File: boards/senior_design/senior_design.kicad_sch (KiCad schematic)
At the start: 55 parts

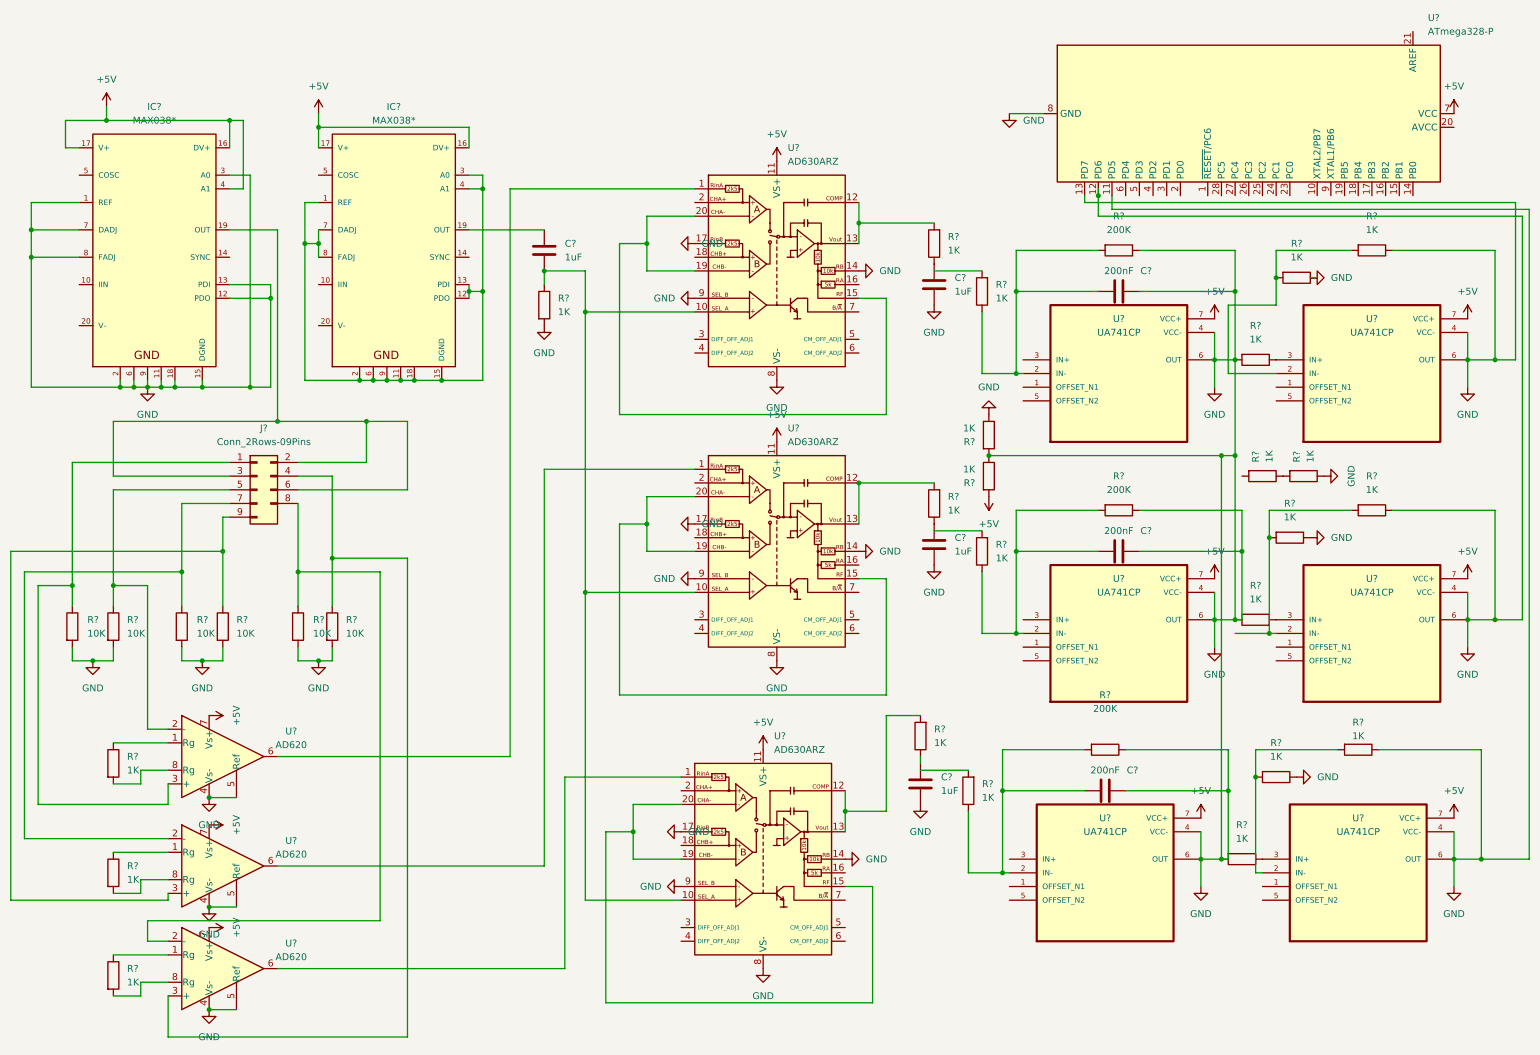
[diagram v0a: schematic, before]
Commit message: added footprints, fixed error in schematic, started PCB layout
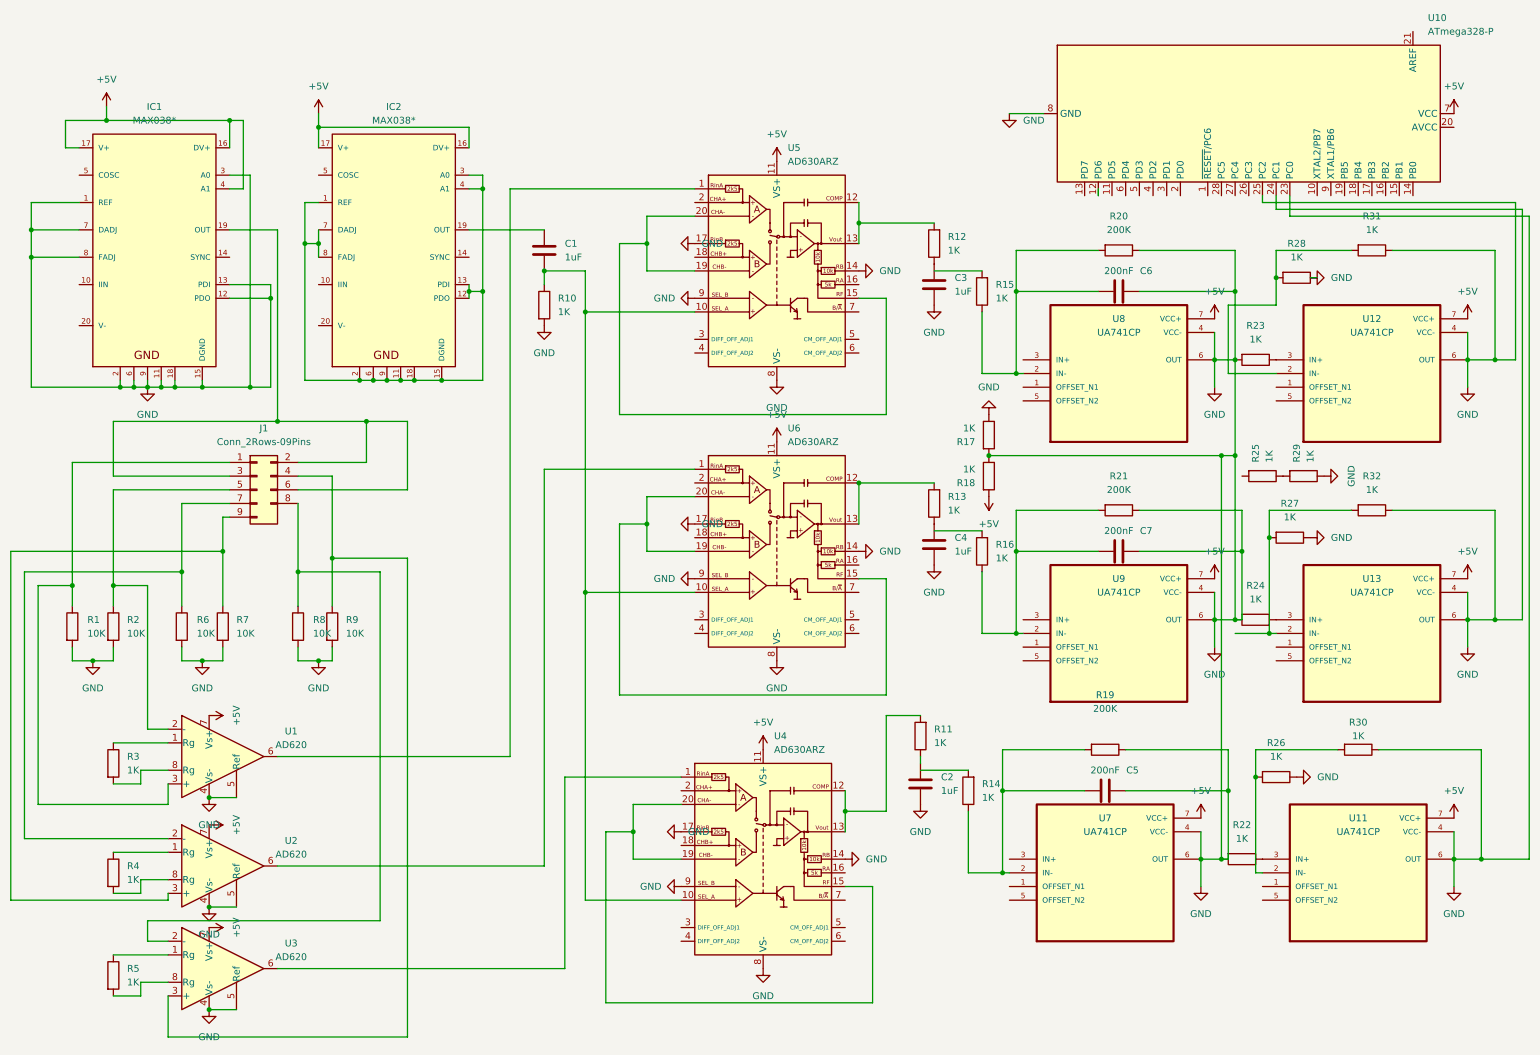
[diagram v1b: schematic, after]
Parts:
- C1, C2, C3, C4, C5, C6, C7: renamed from C?; footprint (none) -> Capacitor_SMD:C_0805_2012Metric_Pad1.18x1.45mm_HandSolder
- IC1, IC2: renamed from IC?; footprint (none) -> MAX038:DIL20
- J1: renamed from J?; footprint (none) -> Connector_Molex:Molex_KK-254_AE-6410-09A_1x09_P2.54mm_Vertical
- R1, R10, R11, R12, R13, R14, R15, R16, R17, R18, R19, R2, R20, R21, R22, R23, R24, R25, R26, R27, R28, R29, R3, R30, R31, R32, R4, R5, R6, R7, R8, R9: renamed from R?; footprint (none) -> Resistor_SMD:R_0805_2012Metric_Pad1.20x1.40mm_HandSolder
- U1, U2, U3: renamed from U?; footprint (none) -> AD620:DIL08
- U11, U12, U13, U7, U8, U9: renamed from U?; footprint DIP794W45P254L959H508Q8 -> uA741:DIP794W45P254L959H508Q8
- gave numbers to parts that had none: 4
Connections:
- net GND: now also U10.23 (PC0), U10.24 (PC1), U10.25 (PC2); no longer U10.11 (PD5), U10.12 (PD6), U10.13 (PD7)

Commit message: changed schematic for 4 boards instead of 1
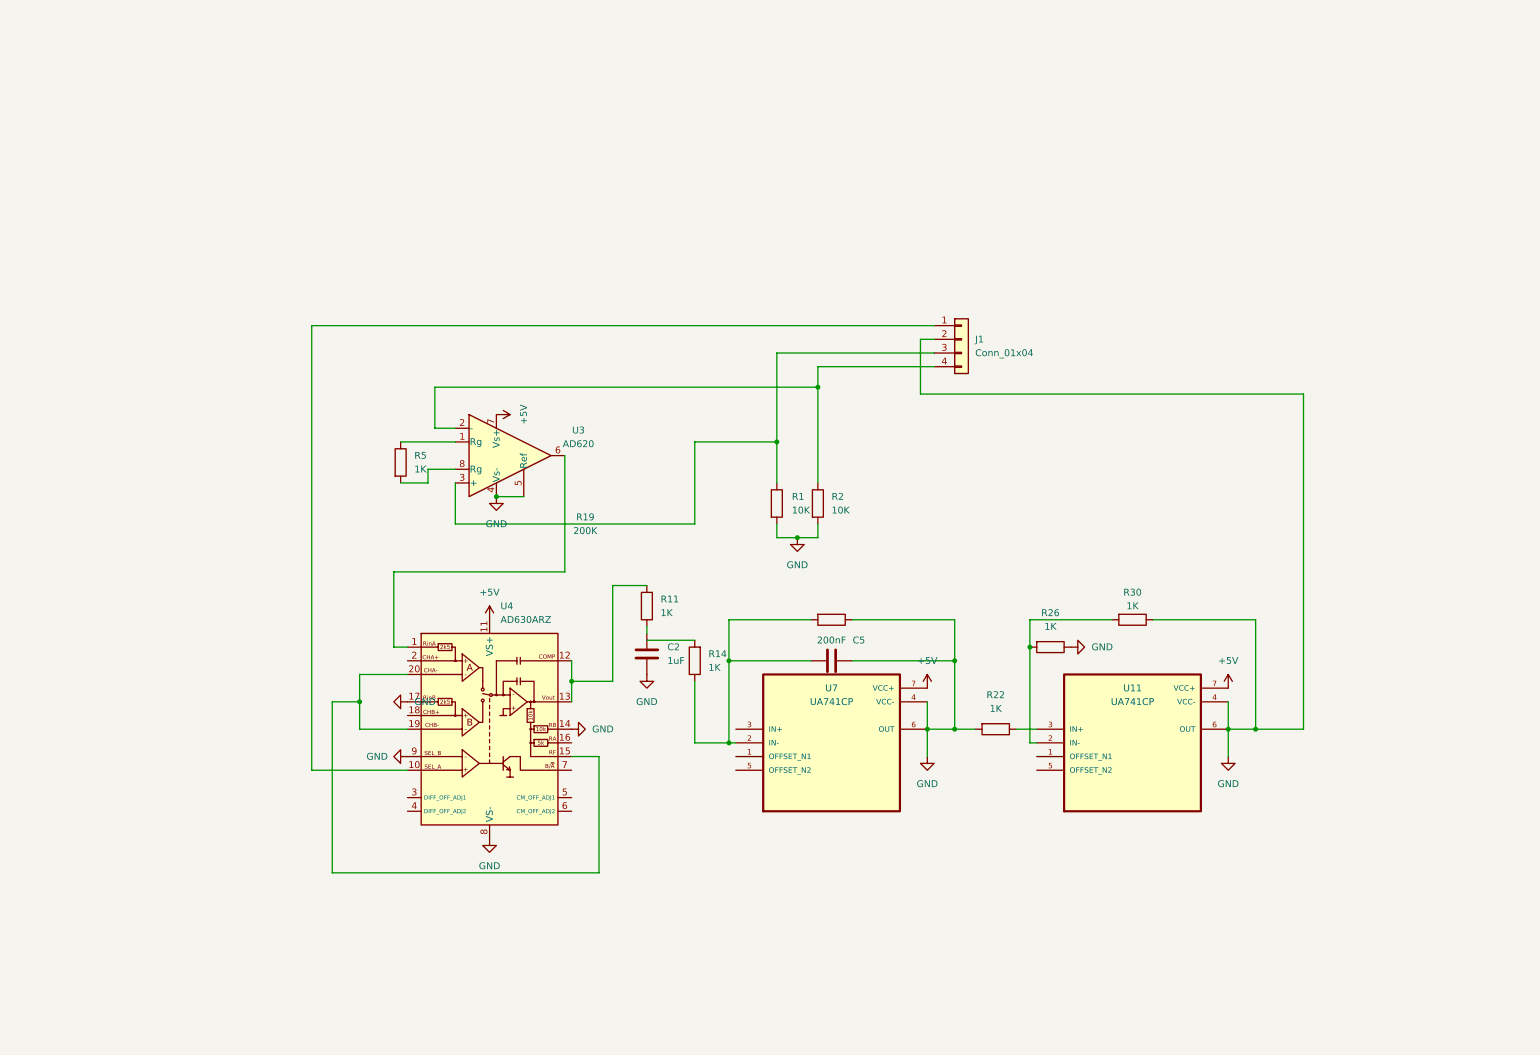
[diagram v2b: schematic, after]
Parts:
- removed C1, C3, C4: 1uF, Capacitor_SMD:C_0805_2012Metric_Pad1.18x1.45mm_HandSolder, symbol Device:C
- removed C6, C7: 200nF, Capacitor_SMD:C_0805_2012Metric_Pad1.18x1.45mm_HandSolder, symbol Device:C
- removed IC1, IC2: MAX038*, MAX038:DIL20, symbol MAX038_:MAX038*
- removed J1: Conn_2Rows-09Pins, Connector_Molex:Molex_KK-254_AE-6410-09A_1x09_P2.54mm_Vertical, symbol Connector_Generic:Conn_2Rows-09Pins
- removed R10, R12, R13, R15, R16, R17, R18, R23, R24, R25, R27, R28, R29, R3, R31, R32, R4: 1K, Resistor_SMD:R_0805_2012Metric_Pad1.20x1.40mm_HandSolder, symbol Device:R
- removed R20, R21: 200K, Resistor_SMD:R_0805_2012Metric_Pad1.20x1.40mm_HandSolder, symbol Device:R
- removed R6, R7, R8, R9: 10K, Resistor_SMD:R_0805_2012Metric_Pad1.20x1.40mm_HandSolder, symbol Device:R
- removed U1, U2: AD620, AD620:DIL08, symbol Amplifier_Instrumentation:AD620
- removed U10: ATmega328-P, Package_DIP:DIP-28_W7.62mm, symbol MCU_Microchip_ATmega:ATmega328-P
- removed U12, U13, U8, U9: UA741CP, uA741:DIP794W45P254L959H508Q8, symbol uA741:UA741CP
- removed U5, U6: AD630ARZ, Package_SO:SOIC-20W_7.5x12.8mm_P1.27mm, symbol Analog:AD630ARZ
- added J1: Conn_01x04, Connector_Molex:Molex_KK-254_AE-6410-04A_1x04_P2.54mm_Vertical, symbol Connector_Generic:Conn_01x04
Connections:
- net GND: now also J1.2 (Pin_2)
- net at U4.10 (SEL_A): now also J1.1 (Pin_1)
- net at R1.1: now also U3.3 (+), J1.3 (Pin_3)
- net at R2.1: now also U3.2 (-), J1.4 (Pin_4)
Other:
- moved on the sheet: C2, C5, R1, R11, R14, R19, R2, R22, R26, R30, R5, U11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
